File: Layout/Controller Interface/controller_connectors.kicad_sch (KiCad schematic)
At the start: 16 parts, among them J2 DIN-7_CenterPin7, J3 DIN-7_CenterPin7, J4 DIN-7_CenterPin7, J7 DIN-7_CenterPin7

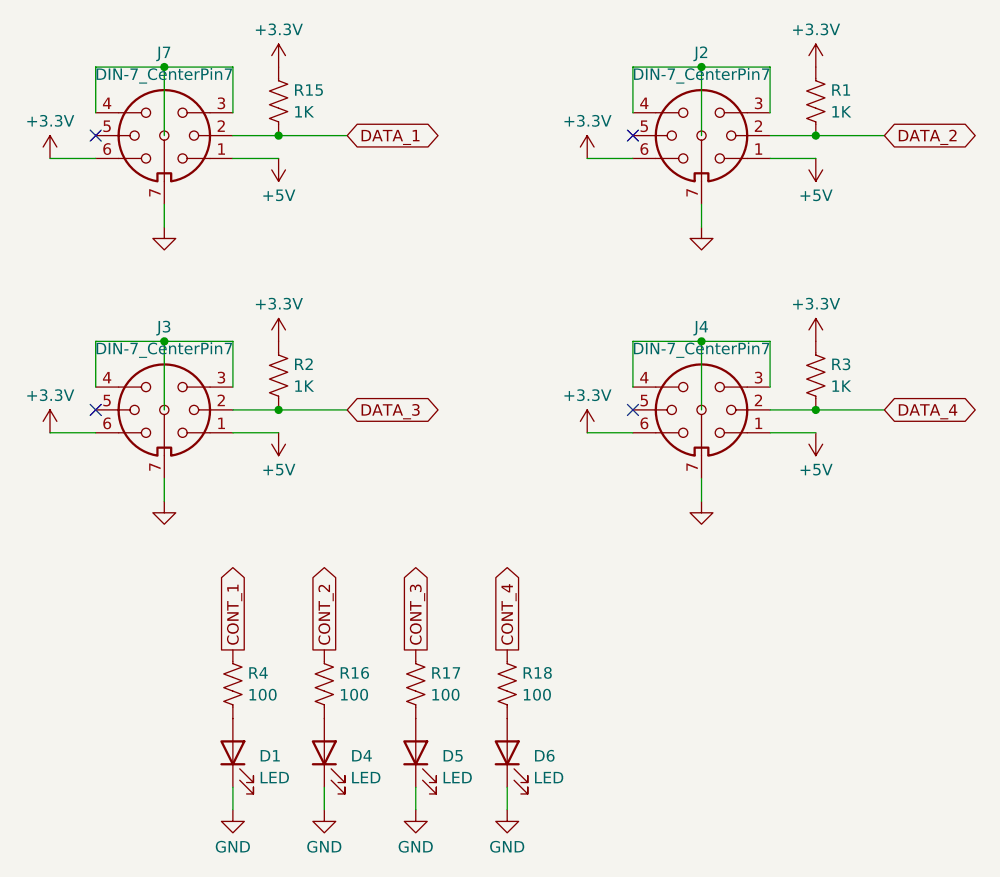
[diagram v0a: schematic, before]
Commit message: Schematic updates
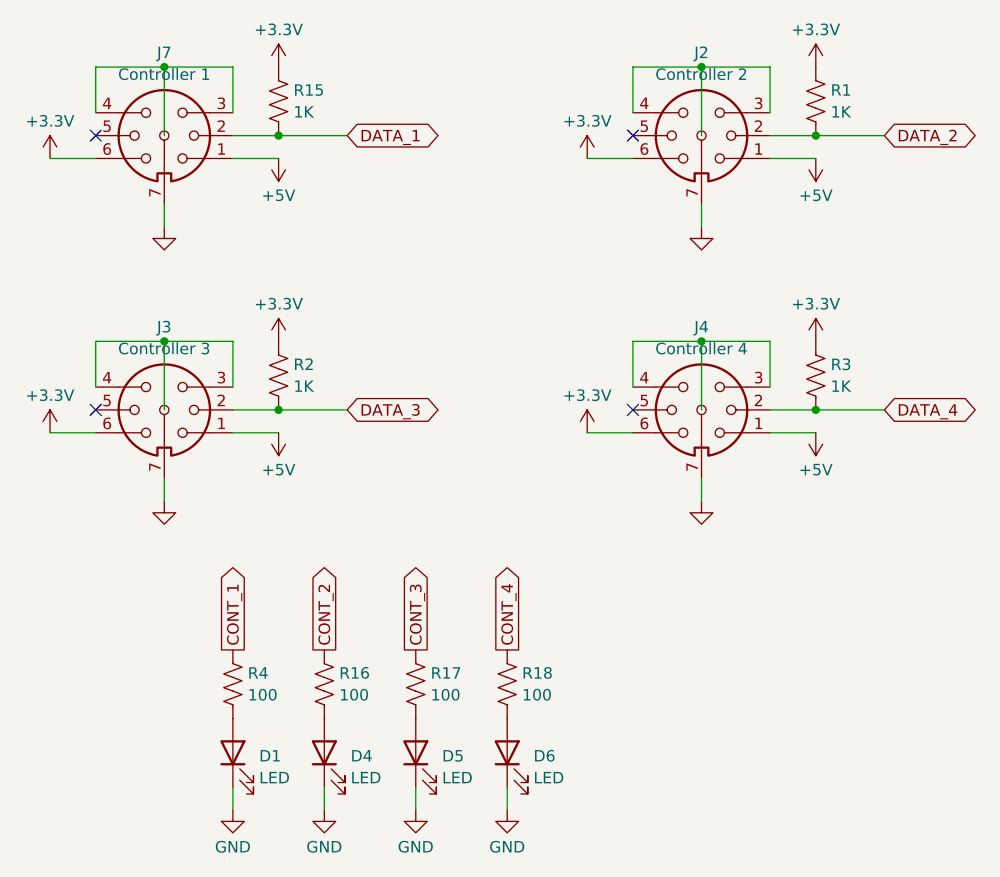
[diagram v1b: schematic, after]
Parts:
- D1, D4, D5, D6: footprint (none) -> LED_SMD:LED_0805_2012Metric
- J2: value DIN-7_CenterPin7 -> Controller 2
- J3: value DIN-7_CenterPin7 -> Controller 3
- J4: value DIN-7_CenterPin7 -> Controller 4
- J7: value DIN-7_CenterPin7 -> Controller 1
- R1, R15, R16, R17, R18, R2, R3, R4: footprint (none) -> Resistor_SMD:R_0805_2012Metric
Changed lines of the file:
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@@
       (effects (font (size 1.27 1.27)) (justify left))
     )
-    (property "Footprint" "" (at 183.896 71.374 90)
+    (property "Footprint" "Resistor_SMD:R_0805_2012Metric" (at 183.896 71.374 90)
       (effects (font (size 1.27 1.27)) hide)
     )
@@
       (effects (font (size 1.27 1.27)) (justify left))
     )
-    (property "Footprint" "" (at 124.206 71.374 90)
+    (property "Footprint" "Resistor_SMD:R_0805_2012Metric" (at 124.206 71.374 90)
       (effects (font (size 1.27 1.27)) hide)
     )
@@
       (effects (font (size 1.27 1.27)) (justify left))
     )
-    (property "Footprint" "" (at 139.446 136.144 90)
+    (property "Footprint" "Resistor_SMD:R_0805_2012Metric" (at 139.446 136.144 90)
       (effects (font (size 1.27 1.27)) hide)
     )
@@
       (effects (font (size 1.27 1.27)))
     )
-    (property "Value" "DIN-7_CenterPin7" (at 110.4901 98.632 0)
+    (property "Value" "Controller 3" (at 110.4901 98.632 0)
       (effects (font (size 1.27 1.27)))
     )
@@
       (effects (font (size 1.27 1.27)) (justify left))
     )
-    (property "Footprint" "" (at 119.126 136.144 90)
+    (property "Footprint" "Resistor_SMD:R_0805_2012Metric" (at 119.126 136.144 90)
       (effects (font (size 1.27 1.27)) hide)
     )
@@
       (effects (font (size 1.27 1.27)) (justify left))
     )
-    (property "Footprint" "" (at 124.206 101.854 90)
+    (property "Footprint" "Resistor_SMD:R_0805_2012Metric" (at 124.206 101.854 90)
       (effects (font (size 1.27 1.27)) hide)
     )
@@
       (effects (font (size 1.27 1.27)) (justify left))
     )
-    (property "Footprint" "" (at 183.896 101.854 90)
+    (property "Footprint" "Resistor_SMD:R_0805_2012Metric" (at 183.896 101.854 90)
       (effects (font (size 1.27 1.27)) hide)
     )
@@
       (effects (font (size 1.27 1.27)) (justify left))
     )
-    (property "Footprint" "" (at 149.606 136.144 90)
+    (property "Footprint" "Resistor_SMD:R_0805_2012Metric" (at 149.606 136.144 90)
       (effects (font (size 1.27 1.27)) hide)
     )
@@
       (effects (font (size 1.27 1.27)) (justify right))
     )
-    (property "Footprint" "" (at 138.43 143.51 0)
+    (property "Footprint" "LED_SMD:LED_0805_2012Metric" (at 138.43 143.51 0)
       (effects (font (size 1.27 1.27)) hide)
     )
@@
       (effects (font (size 1.27 1.27)) (justify right))
     )
-    (property "Footprint" "" (at 128.27 143.51 0)
+    (property "Footprint" "LED_SMD:LED_0805_2012Metric" (at 128.27 143.51 0)
       (effects (font (size 1.27 1.27)) hide)
     )
@@
       (effects (font (size 1.27 1.27)) (justify right))
     )
-    (property "Footprint" "" (at 118.11 143.51 0)
+    (property "Footprint" "LED_SMD:LED_0805_2012Metric" (at 118.11 143.51 0)
       (effects (font (size 1.27 1.27)) hide)
     )
@@
       (effects (font (size 1.27 1.27)))
     )
-    (property "Value" "DIN-7_CenterPin7" (at 110.4901 68.152 0)
+    (property "Value" "Controller 1" (at 110.4901 68.152 0)
       (effects (font (size 1.27 1.27)))
     )
@@
       (effects (font (size 1.27 1.27)) (justify left))
     )
-    (property "Footprint" "" (at 129.286 136.144 90)
+    (property "Footprint" "Resistor_SMD:R_0805_2012Metric" (at 129.286 136.144 90)
       (effects (font (size 1.27 1.27)) hide)
     )
@@
       (effects (font (size 1.27 1.27)))
     )
-    (property "Value" "DIN-7_CenterPin7" (at 170.1801 68.152 0)
+    (property "Value" "Controller 2" (at 170.1801 68.152 0)
       (effects (font (size 1.27 1.27)))
     )
@@
       (effects (font (size 1.27 1.27)) (justify right))
     )
-    (property "Footprint" "" (at 148.59 143.51 0)
+    (property "Footprint" "LED_SMD:LED_0805_2012Metric" (at 148.59 143.51 0)
       (effects (font (size 1.27 1.27)) hide)
     )
@@
       (effects (font (size 1.27 1.27)))
     )
-    (property "Value" "DIN-7_CenterPin7" (at 170.1801 98.632 0)
-      (effects (font (size 1.27 1.27)))
-    )
+    (property "Value" "Controller 4" (at 170.1801 98.632 0)
+      (effects (font (size 1.27 1.27)))
+    )

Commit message: Completed schematic and layout
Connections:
- net GND: now also J2.3, J2.4, J3.3, J3.4, J4.3, J4.4, J7.3, J7.4
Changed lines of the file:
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@@
 (kicad_sch (version 20230121) (generator eeschema)
   (paper "A4")
+  (junction (at 110.49 82.55) (diameter 0) (color 0 0 0 0)
+  )
+  (junction (at 170.18 82.55) (diameter 0) (color 0 0 0 0)
+  )
   (junction (at 123.19 105.41) (diameter 0) (color 0 0 0 0)
   )
-  (junction (at 170.18 97.79) (diameter 0) (color 0 0 0 0)
+  (junction (at 110.49 113.03) (diameter 0) (color 0 0 0 0)
   )
   (junction (at 110.49 97.79) (diameter 0) (color 0 0 0 0)
+  )
+  (junction (at 170.18 97.79) (diameter 0) (color 0 0 0 0)
   )
   (junction (at 110.49 67.31) (diameter 0) (color 0 0 0 0)
@@
   )
   (junction (at 170.18 67.31) (diameter 0) (color 0 0 0 0)
+  )
+  (junction (at 170.18 113.03) (diameter 0) (color 0 0 0 0)
   )
   (no_connect (at 102.87 105.41))
@@
     (stroke (width 0) (type default))
   )
-  (wire (pts (xy 110.49 67.31) (xy 118.11 67.31))
+  (wire (pts (xy 102.87 67.31) (xy 110.49 67.31))
     (stroke (width 0) (type default))
   )
@@
     (stroke (width 0) (type default))
   )
-  (wire (pts (xy 170.18 97.79) (xy 170.18 105.41))
-    (stroke (width 0) (type default))
-  )
   (wire (pts (xy 177.8 105.41) (xy 182.88 105.41))
     (stroke (width 0) (type default))
@@
     (stroke (width 0) (type default))
   )
-  (wire (pts (xy 110.49 97.79) (xy 118.11 97.79))
-    (stroke (width 0) (type default))
-  )
-  (wire (pts (xy 102.87 67.31) (xy 110.49 67.31))
+  (wire (pts (xy 102.87 97.79) (xy 110.49 97.79))
     (stroke (width 0) (type default))
   )
@@
     (stroke (width 0) (type default))
   )
-  (wire (pts (xy 110.49 67.31) (xy 110.49 74.93))
+  (wire (pts (xy 110.49 113.03) (xy 110.49 115.57))
+    (stroke (width 0) (type default))
+  )
+  (wire (pts (xy 110.49 67.31) (xy 118.11 67.31))
     (stroke (width 0) (type default))
   )
   (wire (pts (xy 118.11 147.32) (xy 118.11 149.86))
+    (stroke (width 0) (type default))
+  )
+  (wire (pts (xy 110.49 67.31) (xy 110.49 82.55))
     (stroke (width 0) (type default))
   )
@@
   )
   (wire (pts (xy 182.88 105.41) (xy 190.5 105.41))
-    (stroke (width 0) (type default))
-  )
-  (wire (pts (xy 170.18 67.31) (xy 170.18 74.93))
-    (stroke (width 0) (type default))
-  )
-  (wire (pts (xy 110.49 113.03) (xy 110.49 115.57))
     (stroke (width 0) (type default))
   )
@@
     (stroke (width 0) (type default))
   )
-  (wire (pts (xy 110.49 97.79) (xy 110.49 105.41))
-    (stroke (width 0) (type default))
-  )
   (wire (pts (xy 157.48 77.47) (xy 162.56 77.47))
     (stroke (width 0) (type default))
@@
     (stroke (width 0) (type default))
   )
-  (wire (pts (xy 118.11 97.79) (xy 118.11 102.87))
+  (wire (pts (xy 170.18 67.31) (xy 170.18 82.55))
     (stroke (width 0) (type default))
   )
-  (wire (pts (xy 102.87 97.79) (xy 110.49 97.79))
+  (wire (pts (xy 118.11 97.79) (xy 118.11 102.87))
     (stroke (width 0) (type default))
   )
@@
   )
   (wire (pts (xy 170.18 67.31) (xy 177.8 67.31))
+    (stroke (width 0) (type default))
+  )
+  (wire (pts (xy 110.49 97.79) (xy 118.11 97.79))
     (stroke (width 0) (type default))
   )
@@
     (stroke (width 0) (type default))
   )
+  (wire (pts (xy 170.18 97.79) (xy 170.18 113.03))
+    (stroke (width 0) (type default))
+  )
   (wire (pts (xy 177.8 74.93) (xy 182.88 74.93))
     (stroke (width 0) (type default))
@@
     (stroke (width 0) (type default))
   )
+  (wire (pts (xy 110.49 97.79) (xy 110.49 113.03))
+    (stroke (width 0) (type default))
+  )

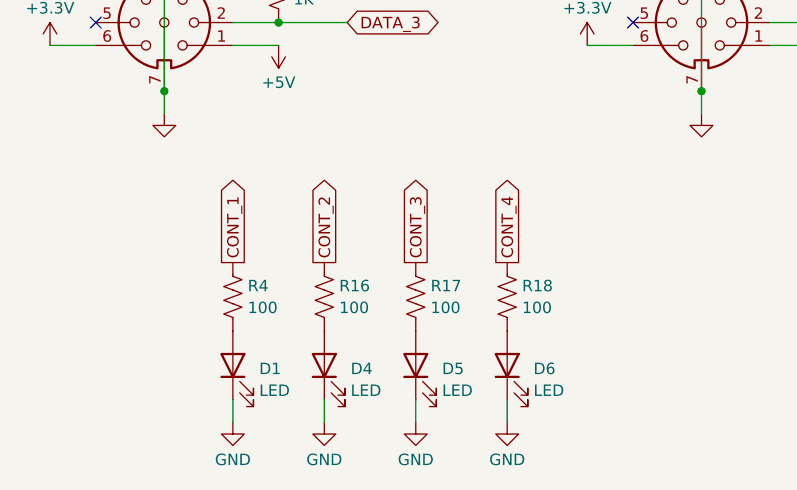
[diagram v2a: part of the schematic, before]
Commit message: Create a separate board for the LEDs
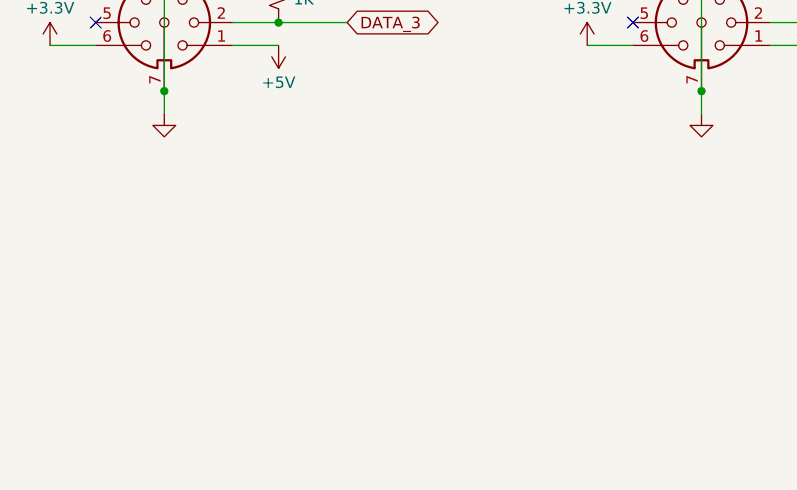
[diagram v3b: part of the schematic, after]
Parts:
- removed D1, D4, D5, D6: LED, LED_SMD:LED_0805_2012Metric, symbol Device:LED
- removed R16, R17, R18, R4: 100, Resistor_SMD:R_0805_2012Metric, symbol Device:R_US

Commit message: Use separate board for lights
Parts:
- R1, R15, R2, R3: footprint Resistor_SMD:R_0805_2012Metric -> Resistor_SMD:R_0603_1608Metric
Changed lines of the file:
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@@
       (effects (font (size 1.27 1.27)) (justify left))
     )
-    (property "Footprint" "Resistor_SMD:R_0805_2012Metric" (at 183.896 71.374 90)
+    (property "Footprint" "Resistor_SMD:R_0603_1608Metric" (at 183.896 71.374 90)
       (effects (font (size 1.27 1.27)) hide)
     )
@@
       (effects (font (size 1.27 1.27)) (justify left))
     )
-    (property "Footprint" "Resistor_SMD:R_0805_2012Metric" (at 124.206 71.374 90)
+    (property "Footprint" "Resistor_SMD:R_0603_1608Metric" (at 124.206 71.374 90)
       (effects (font (size 1.27 1.27)) hide)
     )
@@
       (effects (font (size 1.27 1.27)) (justify left))
     )
-    (property "Footprint" "Resistor_SMD:R_0805_2012Metric" (at 124.206 101.854 90)
+    (property "Footprint" "Resistor_SMD:R_0603_1608Metric" (at 124.206 101.854 90)
       (effects (font (size 1.27 1.27)) hide)
     )
@@
       (effects (font (size 1.27 1.27)) (justify left))
     )
-    (property "Footprint" "Resistor_SMD:R_0805_2012Metric" (at 183.896 101.854 90)
+    (property "Footprint" "Resistor_SMD:R_0603_1608Metric" (at 183.896 101.854 90)
       (effects (font (size 1.27 1.27)) hide)
     )
